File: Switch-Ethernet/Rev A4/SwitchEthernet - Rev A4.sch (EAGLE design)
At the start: 118 parts, among them J1 22-05-7028-02, P1 RB1-125BAG1A, T1 H1102FNL, T2 H1102FNL, U1 TC1264-3.3, U2 TC1264-1.8, U3 KSZ8995MA, U4 AT24C02C-SSHM-B, X1 NE8FAV, X2 NE8FAV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

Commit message: Rename .sch and .brd
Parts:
- removed U$5: EXMACHINA-LOGO-NAME, exmachina:EXMACHINA-LOGO-NAME
- removed U$6: CC-BY-NC-SA, cc-by-sa:CC-BY-NC-SA
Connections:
- net L1-1: now also U3B.LED2-0; no longer U3B.LED3-0
- net L1-2: now also U3B.LED2-1; no longer U3B.LED3-1
- net L2-1: now also U3B.LED3-0; no longer U3B.LED1-0
- net L2-2: now also U3B.LED3-1; no longer U3B.LED1-1
- net L3-1: now also U3B.LED1-0; no longer U3B.LED2-0
- net L3-2: now also U3B.LED1-1; no longer U3B.LED2-1
- net RX1_ISO_N: now also U3A.RXM2; no longer U3A.RXM3
- net RX1_ISO_P: now also U3A.RXP2; no longer U3A.RXP3
- net RX2_ISO_N: now also U3A.RXM3; no longer U3A.RXM1
- net RX2_ISO_P: now also U3A.RXP3; no longer U3A.RXP1
- net RX3_ISO_N: now also U3A.RXM1; no longer U3A.RXM2
- net RX3_ISO_P: now also U3A.RXP1; no longer U3A.RXP2
- net TX1_ISO_N: now also U3A.TXM2; no longer U3A.TXM3
- net TX1_ISO_P: now also U3A.TXP2; no longer U3A.TXP3
- net TX2_ISO_N: now also U3A.TXM3; no longer U3A.TXM1
- net TX2_ISO_P: now also U3A.TXP3; no longer U3A.TXP1
- net TX3_ISO_N: now also U3A.TXM1; no longer U3A.TXM2
- net TX3_ISO_P: now also U3A.TXP1; no longer U3A.TXP2

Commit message: Preplace component on the board
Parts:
- added J2: DF17(3.0)-20DP-0.5V(57), con-hirose:DF17(3.0)-20DP-0.5V(57)
- added J3: (no value), con-hirose:DF17(3.0)-20DS-0.5V(57)
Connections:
- net RX2_M renamed RX2_N
- net TX1_M renamed TX1_N
- net TX2_M renamed TX2_N
- removed net RX1_M: T1.RX-, X1.2
- new net CT_1: J2.7, J3.7, R6.2, T1.RXCT, T1.TXCT
- new net CT_2: J2.14, R13.2, T2.RXCT, T2.TXCT
- new net RX1_N: J2.3, J3.3, T1.RX-, X1.2
- net L1-1: now also J2.5, J3.5
- net L1-2: now also J2.6, J3.6
- net L2-1: now also J2.15, J2.16
- net N$1: now also J2.19; no longer R6.2, T1.RXCT, T1.TXCT
- net N$4: now also J2.18; no longer R13.2, T2.RXCT, T2.TXCT
- net RX1_P: now also J2.2, J3.2
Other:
- moved on the sheet: C1, C10, C13, C14, C15, C16, C17, C2, C3, C33, C4, C44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

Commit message: Connect board-to board connector
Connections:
- removed net N$1: J2.19
- removed net N$4: J2.18
- net +3V3: now also J2.1, J3.1
- net CT_1: now also J2.10, J3.10; no longer J2.7, J3.7
- net CT_2: now also J2.11, J3.11; no longer J2.14
- net GND: now also J2.14, J2.17, J2.20, J2.4, J2.7, J3.14, J3.17, J3.20, J3.4, J3.7
- net L1-1: now also J2.8, J3.8; no longer J2.5, J3.5
- net L1-2: now also J2.9, J3.9; no longer J2.6, J3.6
- net L2-1: now also J2.12, J2.13, J3.12, J3.13; no longer J2.15, J2.16
- net RX2_N: now also J2.15, J2.18, J3.15, J3.18
- net RX2_P: now also J2.16, J2.19, J3.16, J3.19
- net TX1_N: now also J2.6, J3.6
- net TX1_P: now also J2.5, J3.5
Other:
- moved on the sheet: LED4, LED5, R41, R42

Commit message: Update connector and route eth 1,2 and 3
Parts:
- J2: value DF17(3.0)-20DP-0.5V(57) -> DF17(2.0)-20DP-0.5V(57); device con-hirose:DF17(3.0)-20DP-0.5V(57) -> con-hirose:DF17(2.0)-20DP-0.5V(57)
- J3: value (none) -> DF17(4.0)-20DP-0.5V(57); device con-hirose:DF17(3.0)-20DS-0.5V(57) -> con-hirose:DF17(4.0)-20DP-0.5V(57)
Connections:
- net +3V3: now also J2-1.P, J3-1.P; no longer J2.1, J3.1
- net CT_1: now also J2-10.P, J3-10.P; no longer J2.10, J3.10
- net CT_2: now also J2-20.P, J3-20.P; no longer J2.11, J3.11
- net GND: now also J2-11.P, J2-14.P, J2-17.P, J2-4.P, J2-7.P, J3-11.P, J3-14.P, J3-17.P, J3-4.P, J3-7.P; no longer J2.14, J2.17, J2.20, J2.4, J2.7, J3.14, J3.17, J3.20, J3.4, J3.7
- net L1-1: now also J2-8.P, J3-8.P; no longer J2.8, J3.8
- net L1-2: now also J2-9.P, J3-9.P; no longer J2.9, J3.9
- net L2-1: now also J2-18.P, J3-18.P; no longer J2.12, J2.13, J3.12, J3.13
- net L2-2: now also J2-19.P, J3-19.P
- net RX1_N: now also J2-3.P, J3-3.P; no longer J2.3, J3.3
- net RX1_P: now also J2-2.P, J3-2.P; no longer J2.2, J3.2
- net RX2_N: now also J2-13.P, J3-13.P; no longer J2.15, J2.18, J3.15, J3.18
- net RX2_P: now also J2-12.P, J3-12.P; no longer J2.16, J2.19, J3.16, J3.19
- net TX1_N: now also J2-6.P, J3-6.P; no longer J2.6, J3.6
- net TX1_P: now also J2-5.P, J3-5.P; no longer J2.5, J3.5
- net TX2_N: now also J2-16.P, J3-16.P
- net TX2_P: now also J2-15.P, J3-15.P
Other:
- note removed: "LED ETHERNET"
- moved on the sheet: LED6, LED7, R43, R44

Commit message: Reroute ETH signals
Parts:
- removed JP1: (no value), pinhead:PINHD-1X5
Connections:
- net GND: no longer JP1.5
- net SCL_CPU: no longer JP1.2
- net SDA_CPU: no longer JP1.3
- net SPIQ_CPU: no longer JP1.1
- net SPIS-N_CPU: no longer JP1.4
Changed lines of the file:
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@@
 <attribute name="OC_NEWARK" value="58K4684"/>
-</part>
-<part name="JP1" library="pinhead" deviceset="PINHD-1X5" device="">
-<attribute name="MF" value=""/>
-<attribute name="MPN" value=""/>
-<attribute name="OC_FARNELL" value="unknown"/>
-<attribute name="OC_NEWARK" value="97K6210"/>
 </part>
 <part name="+1V2" library="supply1" deviceset="+1V8" device=""/>
@@
 <attribute name="OC_FARNELL" x="353.06" y="35.56" size="1.778" layer="96" display="off"/>
 </instance>
-<instance part="JP1" gate="A" x="378.46" y="111.76">
-<attribute name="OC_NEWARK" x="378.46" y="111.76" size="1.778" layer="96" display="off"/>
-<attribute name="MF" x="378.46" y="111.76" size="1.778" layer="96" display="off"/>
-<attribute name="MPN" x="378.46" y="111.76" size="1.778" layer="96" display="off"/>
-<attribute name="OC_FARNELL" x="378.46" y="111.76" size="1.778" layer="96" display="off"/>
-</instance>
 <instance part="+1V2" gate="G$1" x="276.86" y="248.92"/>
 <instance part="+1V6" gate="G$1" x="373.38" y="223.52"/>
@@
 <wire x1="365.76" y1="101.6" x2="365.76" y2="106.68" width="0.1524" layer="91"/>
 <wire x1="365.76" y1="106.68" x2="375.92" y2="106.68" width="0.1524" layer="91"/>
-<pinref part="JP1" gate="A" pin="5"/>
 </segment>
 <segment>
@@
 <wire x1="375.92" y1="116.84" x2="358.14" y2="116.84" width="0.1524" layer="91"/>
 <label x="358.14" y="116.84" size="1.27" layer="95" rot="MR0" xref="yes"/>
-<pinref part="JP1" gate="A" pin="1"/>
 </segment>
 <segment>
@@
 <wire x1="375.92" y1="114.3" x2="358.14" y2="114.3" width="0.1524" layer="91"/>
 <label x="358.14" y="114.3" size="1.27" layer="95" rot="MR0" xref="yes"/>
-<pinref part="JP1" gate="A" pin="2"/>
 </segment>
 <segment>
@@
 <wire x1="375.92" y1="111.76" x2="358.14" y2="111.76" width="0.1524" layer="91"/>
 <label x="358.14" y="111.76" size="1.27" layer="95" rot="MR0" xref="yes"/>
-<pinref part="JP1" gate="A" pin="3"/>
 </segment>
 <segment>
@@
 <wire x1="375.92" y1="109.22" x2="358.14" y2="109.22" width="0.1524" layer="91"/>
 <label x="358.14" y="109.22" size="1.27" layer="95" rot="MR0" xref="yes"/>
-<pinref part="JP1" gate="A" pin="4"/>
-</segment>
-<segment>
+</segment>
+<segment>

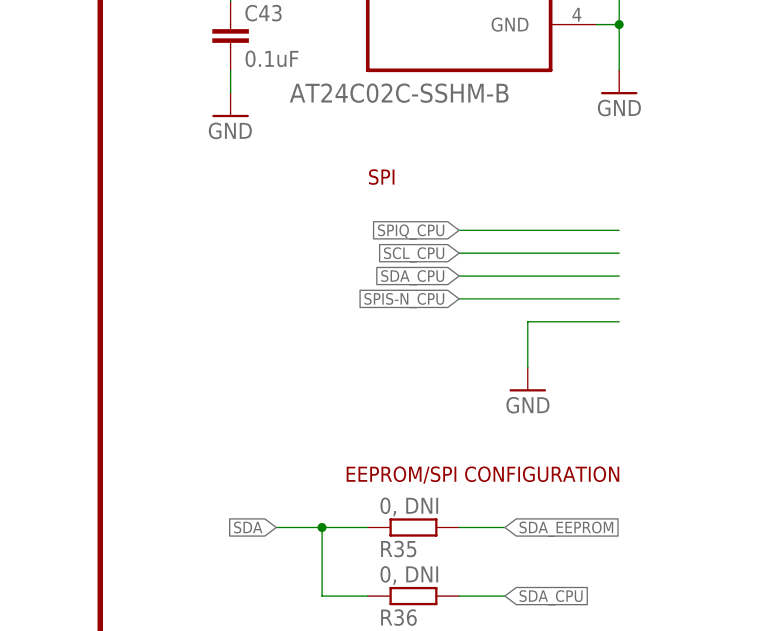
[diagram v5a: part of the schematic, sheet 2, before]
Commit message: Route the spi nets
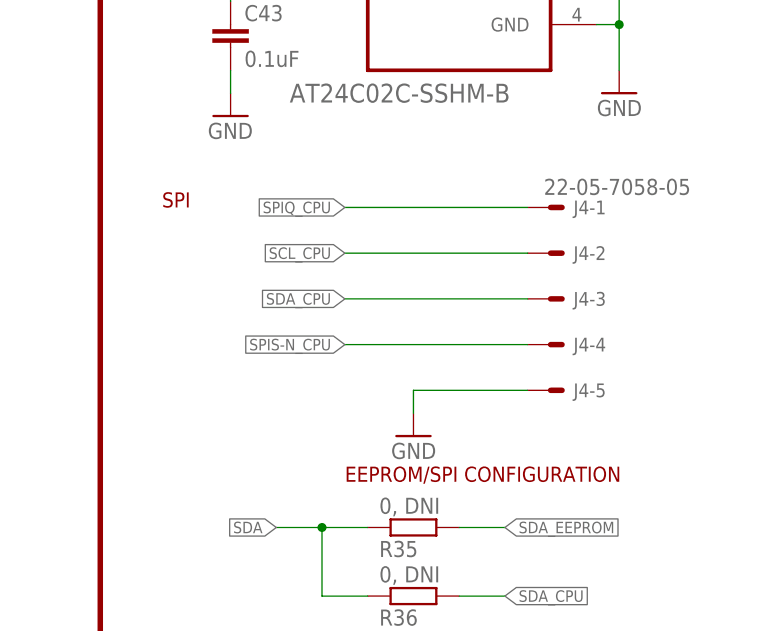
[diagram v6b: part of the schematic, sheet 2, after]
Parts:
- added J4: 22-05-7058-05, con-molex:22-05-7058-05
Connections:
- net GND: now also J4-5.S
- net SCL_CPU: now also J4-2.S
- net SDA_CPU: now also J4-3.S
- net SPIQ_CPU: now also J4-1.S
- net SPIS-N_CPU: now also J4-4.S
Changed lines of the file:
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@@
 <part name="J2" library="con-hirose" deviceset="DF17(?)-20DP-0.5V(57)" device="2.0"/>
 <part name="J3" library="con-hirose" deviceset="DF17(?)-20DP-0.5V(57)" device="4.0"/>
+<part name="J4" library="con-molex" deviceset="22-?-05" device="05-7058"/>
 </parts>
 <sheets>
@@
 <wire x1="318.262" y1="175.26" x2="318.262" y2="24.384" width="0.6096" layer="94"/>
 <text x="345.44" y="167.64" size="1.6764" layer="94">EEPROM</text>
-<text x="347.98" y="121.92" size="1.6764" layer="94">SPI</text>
+<text x="325.12" y="119.38" size="1.6764" layer="94">SPI</text>
 <text x="345.44" y="88.9" size="1.6764" layer="94">EEPROM/SPI CONFIGURATION</text>
 <wire x1="39.116" y1="131.572" x2="4.064" y2="131.572" width="0.6096" layer="94"/>
@@
 <attribute name="OC_FARNELL" x="332.74" y="139.7" size="1.778" layer="96" display="off"/>
 </instance>
-<instance part="GND29" gate="1" x="365.76" y="99.06" rot="MR0"/>
+<instance part="GND29" gate="1" x="353.06" y="93.98" rot="MR0"/>
 <instance part="R35" gate="G$1" x="353.06" y="83.82" rot="MR180">
 <attribute name="OC_NEWARK" x="353.06" y="83.82" size="1.778" layer="96" display="off"/>
@@
 <attribute name="MPN" x="307.34" y="8.89" size="1.778" layer="96" display="off"/>
 </instance>
+<instance part="J4" gate="-1" x="368.3" y="119.38"/>
+<instance part="J4" gate="-2" x="368.3" y="114.3"/>
+<instance part="J4" gate="-3" x="368.3" y="109.22"/>
+<instance part="J4" gate="-4" x="368.3" y="104.14"/>
+<instance part="J4" gate="-5" x="368.3" y="99.06"/>
 </instances>
 <busses>
@@
 <segment>
 <pinref part="GND29" gate="1" pin="GND"/>
-<wire x1="365.76" y1="101.6" x2="365.76" y2="106.68" width="0.1524" layer="91"/>
-<wire x1="365.76" y1="106.68" x2="375.92" y2="106.68" width="0.1524" layer="91"/>
+<wire x1="353.06" y1="96.52" x2="353.06" y2="99.06" width="0.1524" layer="91"/>
+<wire x1="353.06" y1="99.06" x2="365.76" y2="99.06" width="0.1524" layer="91"/>
+<pinref part="J4" gate="-5" pin="S"/>
 </segment>
 <segment>
@@
 <net name="SPIQ_CPU" class="0">
 <segment>
-<wire x1="375.92" y1="116.84" x2="358.14" y2="116.84" width="0.1524" layer="91"/>
-<label x="358.14" y="116.84" size="1.27" layer="95" rot="MR0" xref="yes"/>
+<wire x1="365.76" y1="119.38" x2="345.44" y2="119.38" width="0.1524" layer="91"/>
+<label x="345.44" y="119.38" size="1.27" layer="95" rot="MR0" xref="yes"/>
+<pinref part="J4" gate="-1" pin="S"/>
 </segment>
 <segment>
@@
 <net name="SCL_CPU" class="0">
 <segment>
-<wire x1="375.92" y1="114.3" x2="358.14" y2="114.3" width="0.1524" layer="91"/>
-<label x="358.14" y="114.3" size="1.27" layer="95" rot="MR0" xref="yes"/>
+<wire x1="365.76" y1="114.3" x2="345.44" y2="114.3" width="0.1524" layer="91"/>
+<label x="345.44" y="114.3" size="1.27" layer="95" rot="MR0" xref="yes"/>
+<pinref part="J4" gate="-2" pin="S"/>
 </segment>
 <segment>
@@
 <net name="SDA_CPU" class="0">
 <segment>
-<wire x1="375.92" y1="111.76" x2="358.14" y2="111.76" width="0.1524" layer="91"/>
-<label x="358.14" y="111.76" size="1.27" layer="95" rot="MR0" xref="yes"/>
+<wire x1="365.76" y1="109.22" x2="345.44" y2="109.22" width="0.1524" layer="91"/>
+<label x="345.44" y="109.22" size="1.27" layer="95" rot="MR0" xref="yes"/>
+<pinref part="J4" gate="-3" pin="S"/>
 </segment>
 <segment>
@@
 <net name="SPIS-N_CPU" class="0">
 <segment>
-<wire x1="375.92" y1="109.22" x2="358.14" y2="109.22" width="0.1524" layer="91"/>
-<label x="358.14" y="109.22" size="1.27" layer="95" rot="MR0" xref="yes"/>
-</segment>
-<segment>
+<wire x1="365.76" y1="104.14" x2="345.44" y2="104.14" width="0.1524" layer="91"/>
+<label x="345.44" y="104.14" size="1.27" layer="95" rot="MR0" xref="yes"/>
+<pinref part="J4" gate="-4" pin="S"/>
+</segment>
+<segment>

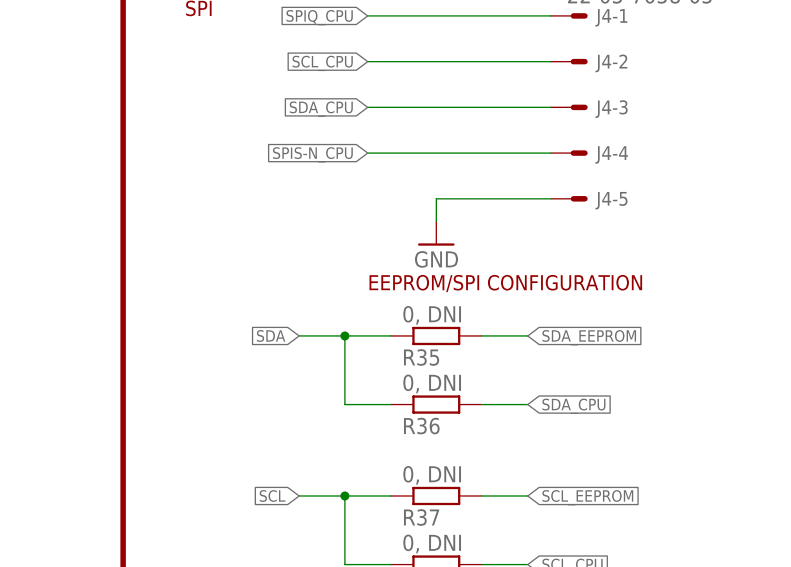
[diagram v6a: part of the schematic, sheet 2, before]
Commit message: Change to the top the RJ45 connector and re-route it
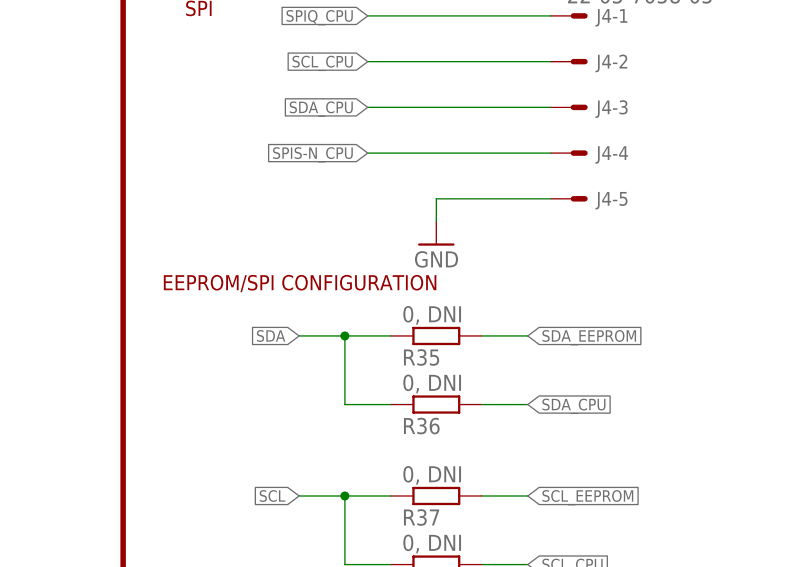
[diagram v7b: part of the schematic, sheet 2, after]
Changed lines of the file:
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@@
 <text x="345.44" y="167.64" size="1.6764" layer="94">EEPROM</text>
 <text x="325.12" y="119.38" size="1.6764" layer="94">SPI</text>
-<text x="345.44" y="88.9" size="1.6764" layer="94">EEPROM/SPI CONFIGURATION</text>
+<text x="322.58" y="88.9" size="1.6764" layer="94">EEPROM/SPI CONFIGURATION</text>
 <wire x1="39.116" y1="131.572" x2="4.064" y2="131.572" width="0.6096" layer="94"/>
 <text x="22.86" y="127" size="2.54" layer="94">RESET</text>
